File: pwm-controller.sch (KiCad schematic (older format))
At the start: 40 parts, among them J1 DEBUG_ADDRESS_I2C_INT, J2 POWER, J3 OUT+, J4 OUT-, SW1 EC12D1524403, U1 STM8S003F3Px, U2 78L05

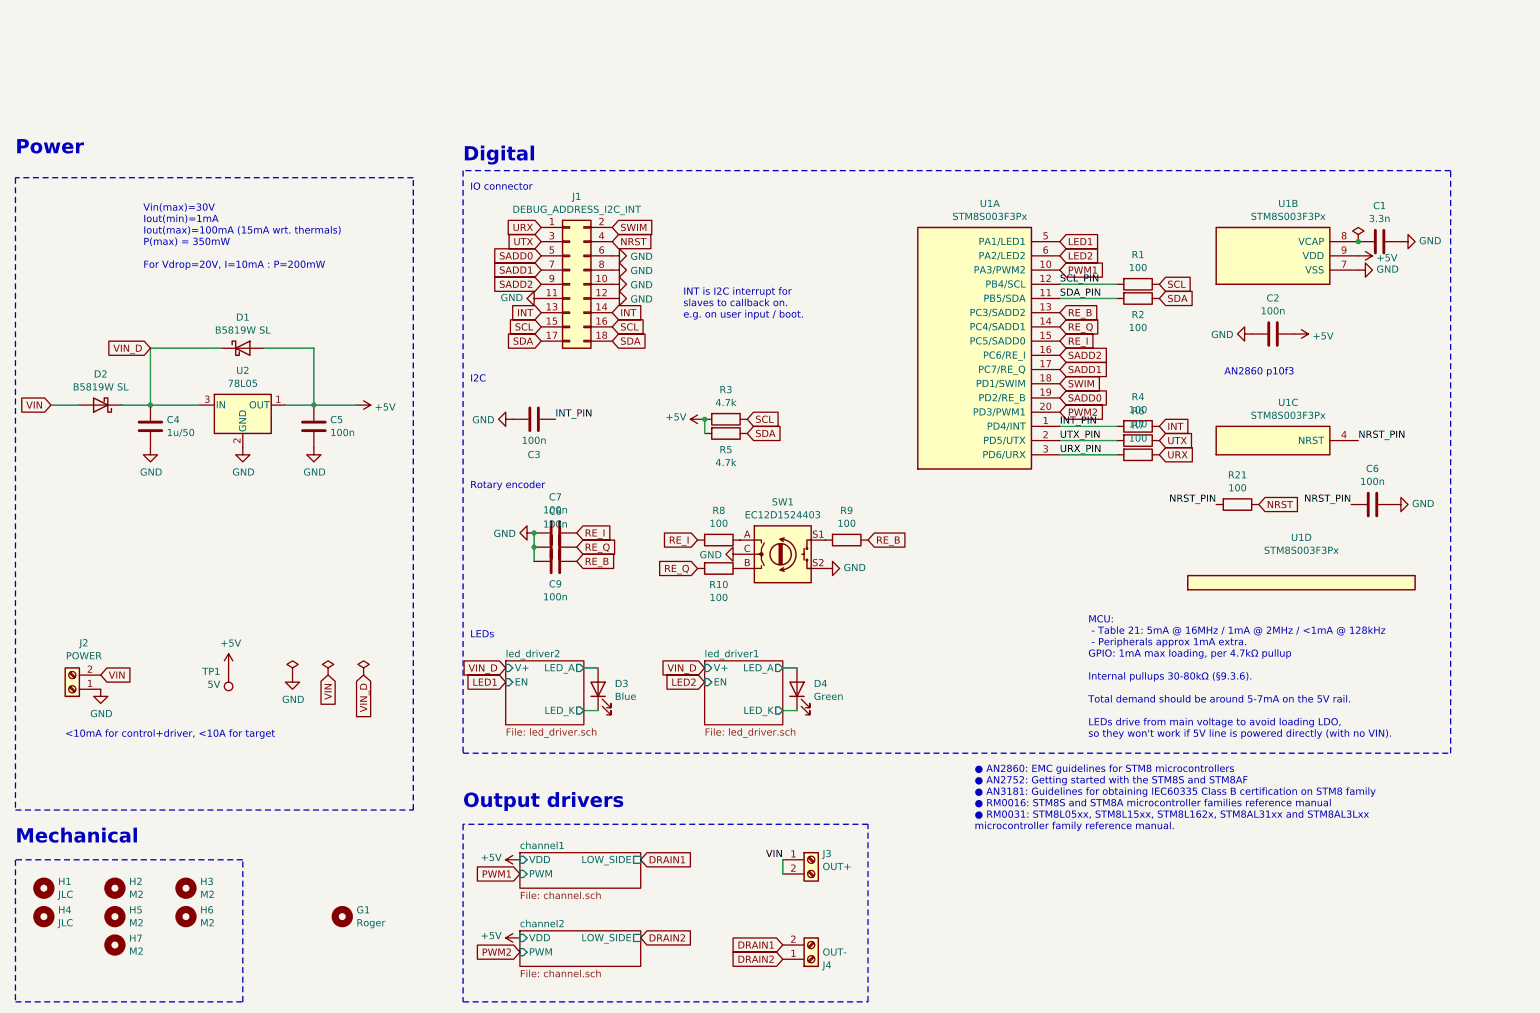
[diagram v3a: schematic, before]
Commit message: Fixed VCAP (3.3nF should be 470...3300nF)
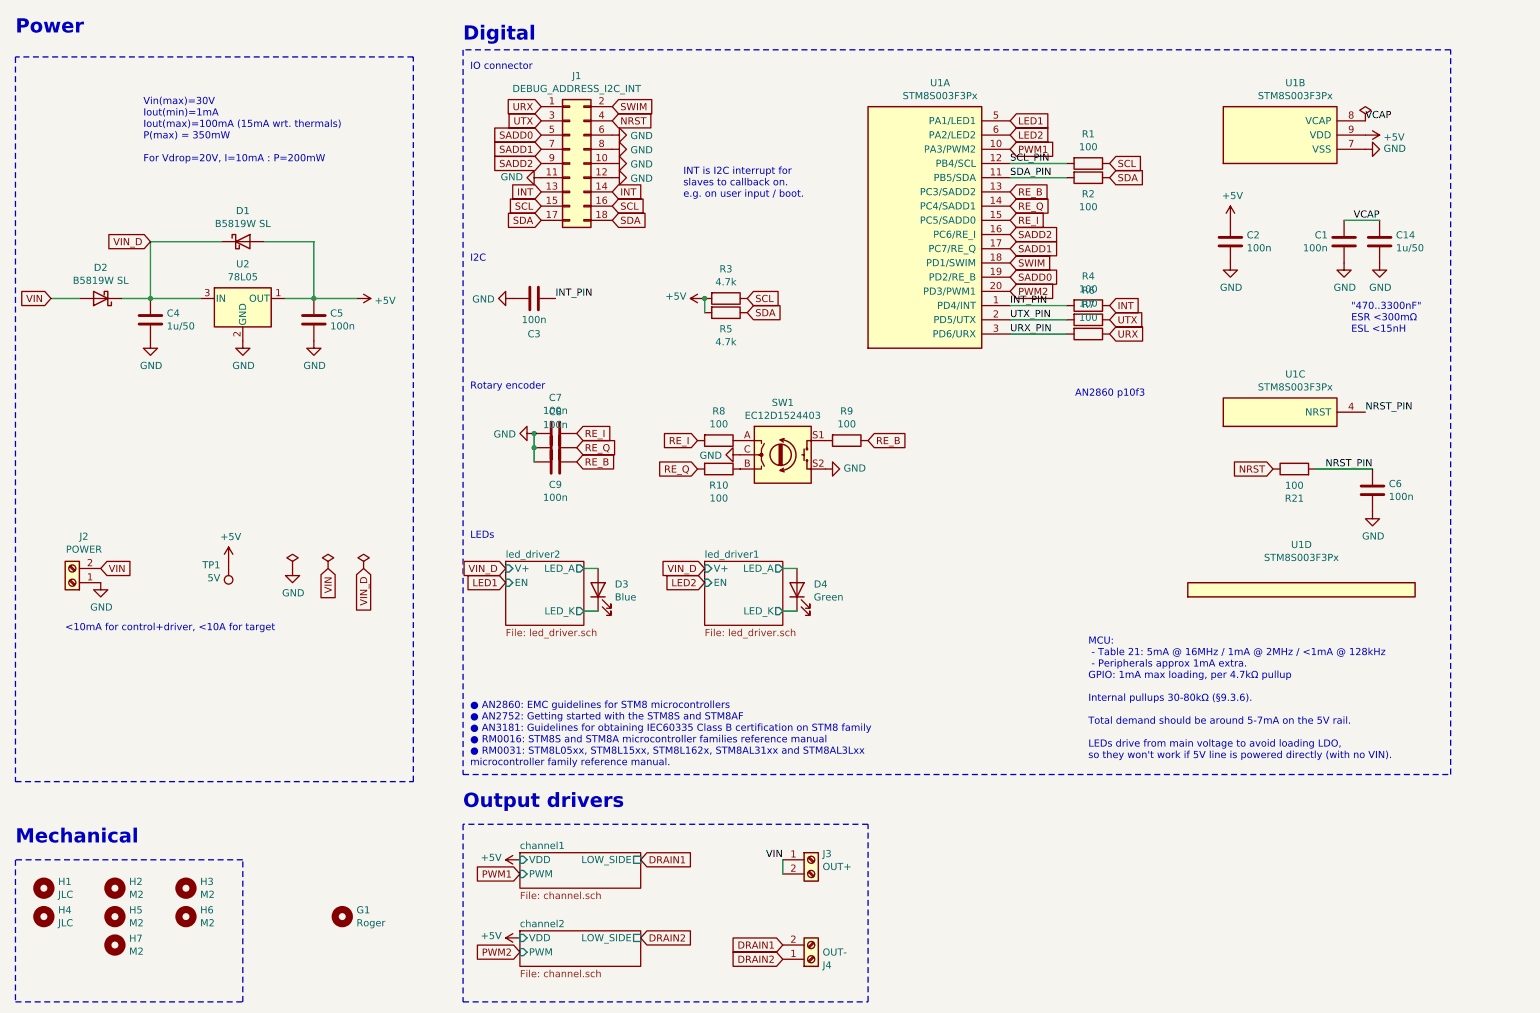
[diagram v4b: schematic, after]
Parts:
- added C14: 1u/50, Capacitor_SMD:C_0603_1608Metric, symbol Device:C
- C1: value 3.3n -> 100n; JLC C26404 -> C1525
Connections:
- net GND: now also C1.1, C14.2; no longer C1.2
- net VCAP: now reaches U1.8 (VCAP)
- net VCAP: now also C1.2, C14.1; no longer C1.1
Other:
- note added: ""470..3300nF"\nESR <300mΩ\nESL <15nH"
- moved on the sheet: C2, C3, C4, C5, C6, C7, C8, C9, D1, D2, D3, D4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
